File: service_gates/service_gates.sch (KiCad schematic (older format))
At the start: 1 part, among them P1 DIN_41612_128P

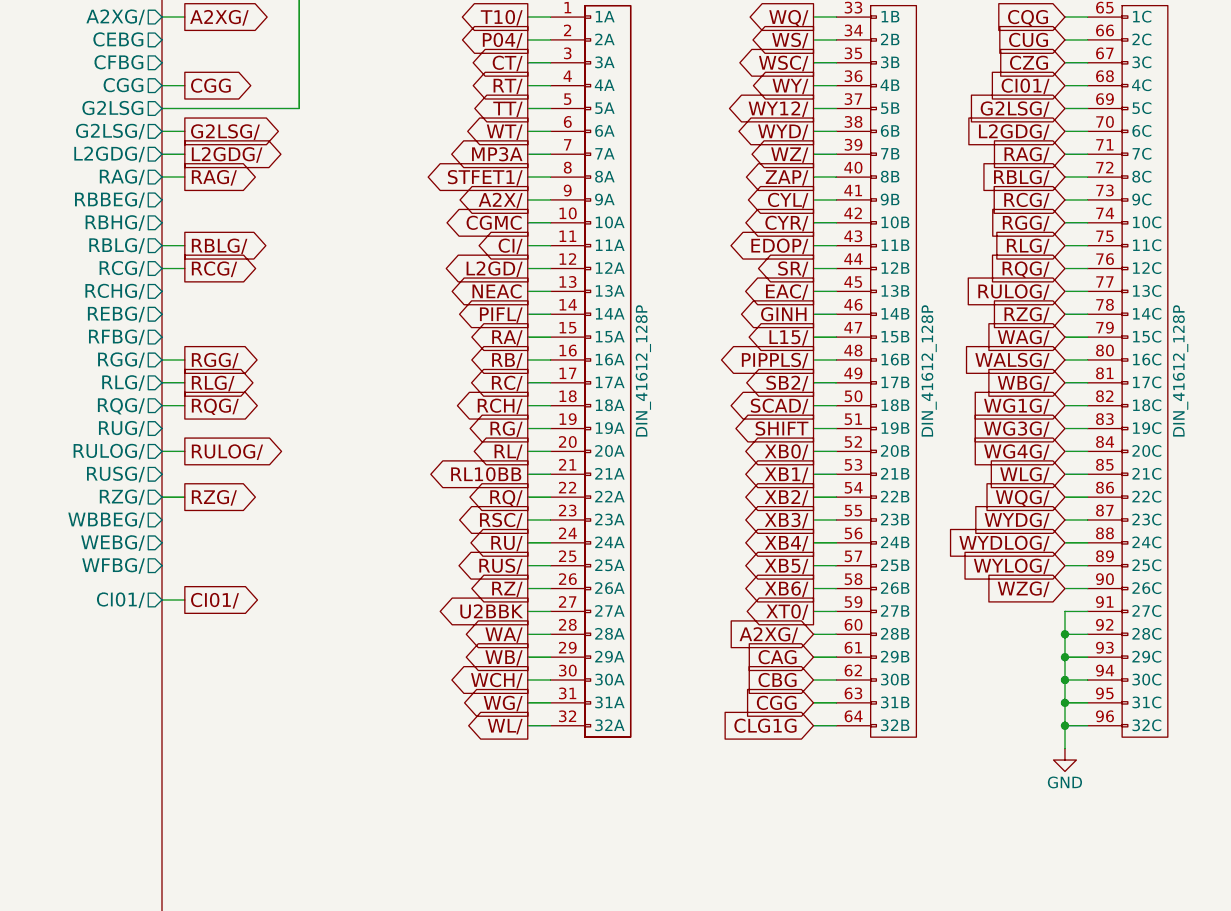
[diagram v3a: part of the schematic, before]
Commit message: Added a fully tied in module 10.
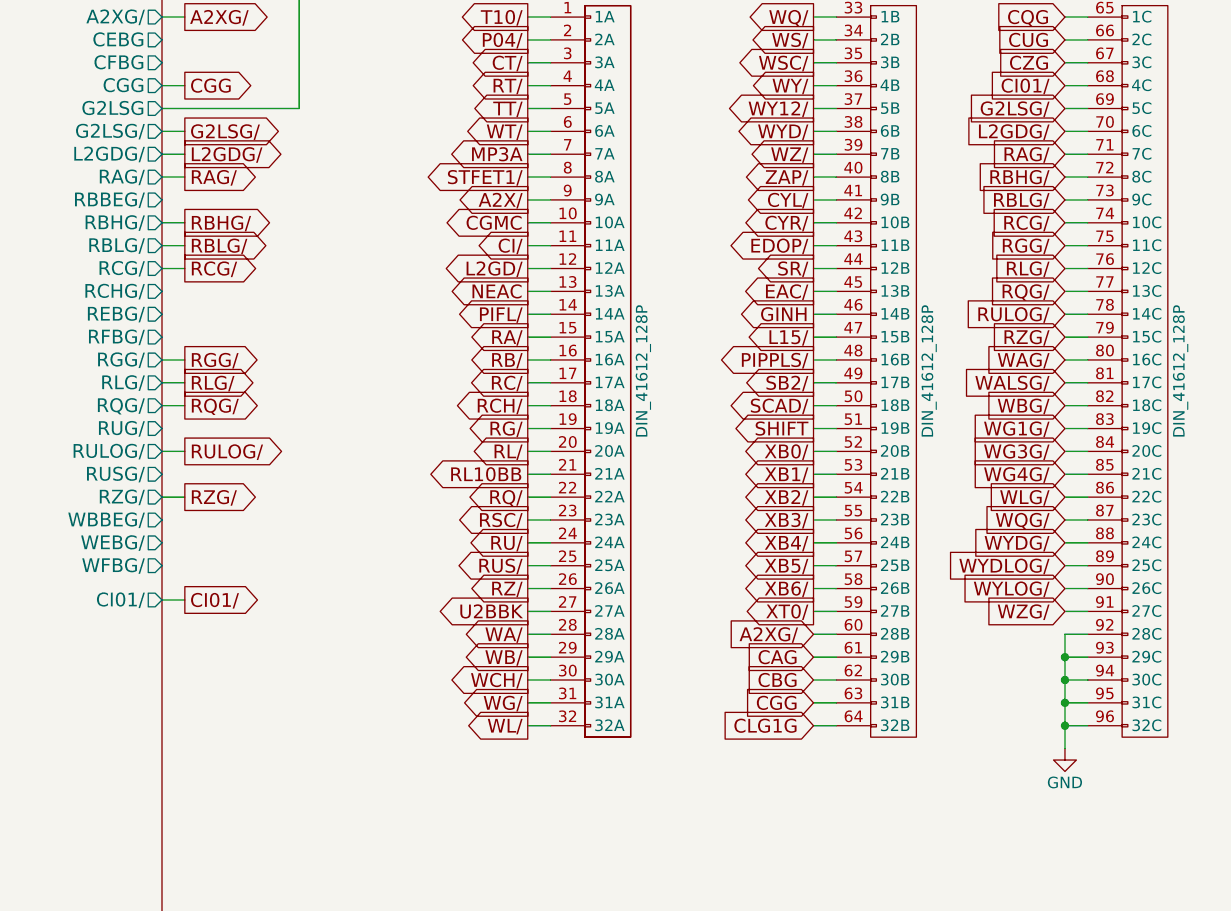
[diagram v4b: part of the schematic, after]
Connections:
- net GND: no longer P1.91 (27C)
- net RBLG/: now also P1.73 (9C); no longer P1.72 (8C)
- net RCG/: now also P1.74 (10C); no longer P1.73 (9C)
- net RGG/: now also P1.75 (11C); no longer P1.74 (10C)
- net RLG/: now also P1.76 (12C); no longer P1.75 (11C)
- net RQG/: now also P1.77 (13C); no longer P1.76 (12C)
- net RULOG/: now also P1.78 (14C); no longer P1.77 (13C)
- net RZG/: now also P1.79 (15C); no longer P1.78 (14C)
- net WAG/: now also P1.80 (16C); no longer P1.79 (15C)
- net WALSG/: now also P1.81 (17C); no longer P1.80 (16C)
- net WBG/: now also P1.82 (18C); no longer P1.81 (17C)
- net WG1G/: now also P1.83 (19C); no longer P1.82 (18C)
- net WG3G/: now also P1.84 (20C); no longer P1.83 (19C)
- net WG4G/: now also P1.85 (21C); no longer P1.84 (20C)
- net WLG/: now also P1.86 (22C); no longer P1.85 (21C)
- net WQG/: now also P1.87 (23C); no longer P1.86 (22C)
- net WYDG/: now also P1.88 (24C); no longer P1.87 (23C)
- net WYDLOG/: now also P1.89 (25C); no longer P1.88 (24C)
- net WYLOG/: now also P1.90 (26C); no longer P1.89 (25C)
- net WZG/: now also P1.91 (27C); no longer P1.90 (26C)
- new net RBHG/: P1.72 (8C)
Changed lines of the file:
@@
 	10600 4150 10700 4150
 Connection ~ 10600 4250
-Wire Wire Line
-	10600 4050 10700 4050
 Connection ~ 10600 4150
 Wire Wire Line
 	10600 3950 10700 3950
-Connection ~ 10600 4050
-Wire Wire Line
-	10600 3850 10700 3850
-Wire Wire Line
-	10600 2650 10700 2650
+Wire Wire Line
+	10600 2750 10700 2750
+Wire Wire Line
+	10600 2550 10700 2550
 Wire Wire Line
 	10600 2450 10700 2450
@@
 Wire Wire Line
 	10600 2250 10700 2250
-Wire Wire Line
-	10600 2150 10700 2150
 $Comp
 L DIN_41612_128P P1
@@
 RBLG/
 Wire Wire Line
-	10600 2050 10700 2050
-Text GLabel 10600 2050 0    60   Input ~ 0
+	10600 2150 10700 2150
+Text GLabel 10600 2150 0    60   Input ~ 0
 RBLG/
 Wire Wire Line
@@
 Text GLabel 6750 2450 2    60   Output ~ 0
 RCG/
-Text GLabel 10600 2150 0    60   Input ~ 0
+Text GLabel 10600 2250 0    60   Input ~ 0
 RCG/
 Wire Wire Line
@@
 Text GLabel 6750 2850 2    60   Output ~ 0
 RGG/
-Text GLabel 10600 2250 0    60   Input ~ 0
+Text GLabel 10600 2350 0    60   Input ~ 0
 RGG/
 Wire Wire Line
@@
 Text GLabel 6750 2950 2    60   Output ~ 0
 RLG/
-Text GLabel 10600 2350 0    60   Input ~ 0
+Text GLabel 10600 2450 0    60   Input ~ 0
 RLG/
 Wire Wire Line
@@
 Text GLabel 6750 3050 2    60   Output ~ 0
 RQG/
-Text GLabel 10600 2450 0    60   Input ~ 0
+Text GLabel 10600 2550 0    60   Input ~ 0
 RQG/
 Wire Wire Line
@@
 RULOG/
 Wire Wire Line
-	10600 2550 10700 2550
-Text GLabel 10600 2550 0    60   Input ~ 0
+	10600 2650 10700 2650
+Text GLabel 10600 2650 0    60   Input ~ 0
 RULOG/
 Wire Wire Line
@@
 Text GLabel 6750 3450 2    60   Output ~ 0
 RZG/
-Text GLabel 10600 2650 0    60   Input ~ 0
+Text GLabel 10600 2750 0    60   Input ~ 0
 RZG/
 Wire Wire Line
@@
 WALSG/
 Wire Wire Line
-	10600 2750 10700 2750
-Text GLabel 10600 2750 0    60   Input ~ 0
-WAG/
-Wire Wire Line
 	10600 2850 10700 2850
 Text GLabel 10600 2850 0    60   Input ~ 0
+WAG/
+Wire Wire Line
+	10600 2950 10700 2950
+Text GLabel 10600 2950 0    60   Input ~ 0
 WALSG/
 Wire Wire Line
@@
 WBG/
 Wire Wire Line
-	10600 2950 10700 2950
-Text GLabel 10600 2950 0    60   Input ~ 0
+	10600 3050 10700 3050
+Text GLabel 10600 3050 0    60   Input ~ 0
 WBG/
 Wire Wire Line
@@
 WG4G/
 Wire Wire Line
-	10600 3050 10700 3050
-Text GLabel 10600 3050 0    60   Input ~ 0
-WG1G/
-Wire Wire Line
 	10600 3150 10700 3150
 Text GLabel 10600 3150 0    60   Input ~ 0
-WG3G/
+WG1G/
 Wire Wire Line
 	10600 3250 10700 3250
 Text GLabel 10600 3250 0    60   Input ~ 0
+WG3G/
+Wire Wire Line
+	10600 3350 10700 3350
+Text GLabel 10600 3350 0    60   Input ~ 0
 WG4G/
 Wire Wire Line
@@
 WLG/
 Wire Wire Line
-	10600 3350 10700 3350
-Text GLabel 10600 3350 0    60   Input ~ 0
-WLG/
-Wire Wire Line
 	10600 3450 10700 3450
 Text GLabel 10600 3450 0    60   Input ~ 0
+WLG/
+Wire Wire Line
+	10600 3550 10700 3550
+Text GLabel 10600 3550 0    60   Input ~ 0
 WQG/
 Wire Wire Line
@@
 WYLOG/
 Wire Wire Line
-	10600 3550 10700 3550
-Text GLabel 10600 3550 0    60   Input ~ 0
-WYDG/
-Wire Wire Line
 	10600 3650 10700 3650
 Text GLabel 10600 3650 0    60   Input ~ 0
-WYDLOG/
+WYDG/
 Wire Wire Line
 	10600 3750 10700 3750
 Text GLabel 10600 3750 0    60   Input ~ 0
+WYDLOG/
+Wire Wire Line
+	10600 3850 10700 3850
+Text GLabel 10600 3850 0    60   Input ~ 0
 WYLOG/
 Wire Wire Line
@@
 WZG/
 Wire Wire Line
-	10600 3950 10600 4550
-Text GLabel 10600 3850 0    60   Input ~ 0
+	10600 4050 10600 4550
+Text GLabel 10600 3950 0    60   Input ~ 0
 WZG/
+Wire Wire Line
+	6650 2250 6750 2250
+Text GLabel 6750 2250 2    60   Output ~ 0
+RBHG/
+Wire Wire Line
+	10600 4050 10700 4050
+Wire Wire Line
+	10600 2050 10700 2050
+Text GLabel 10600 2050 0    60   Input ~ 0
+RBHG/
 $EndSCHEMATC

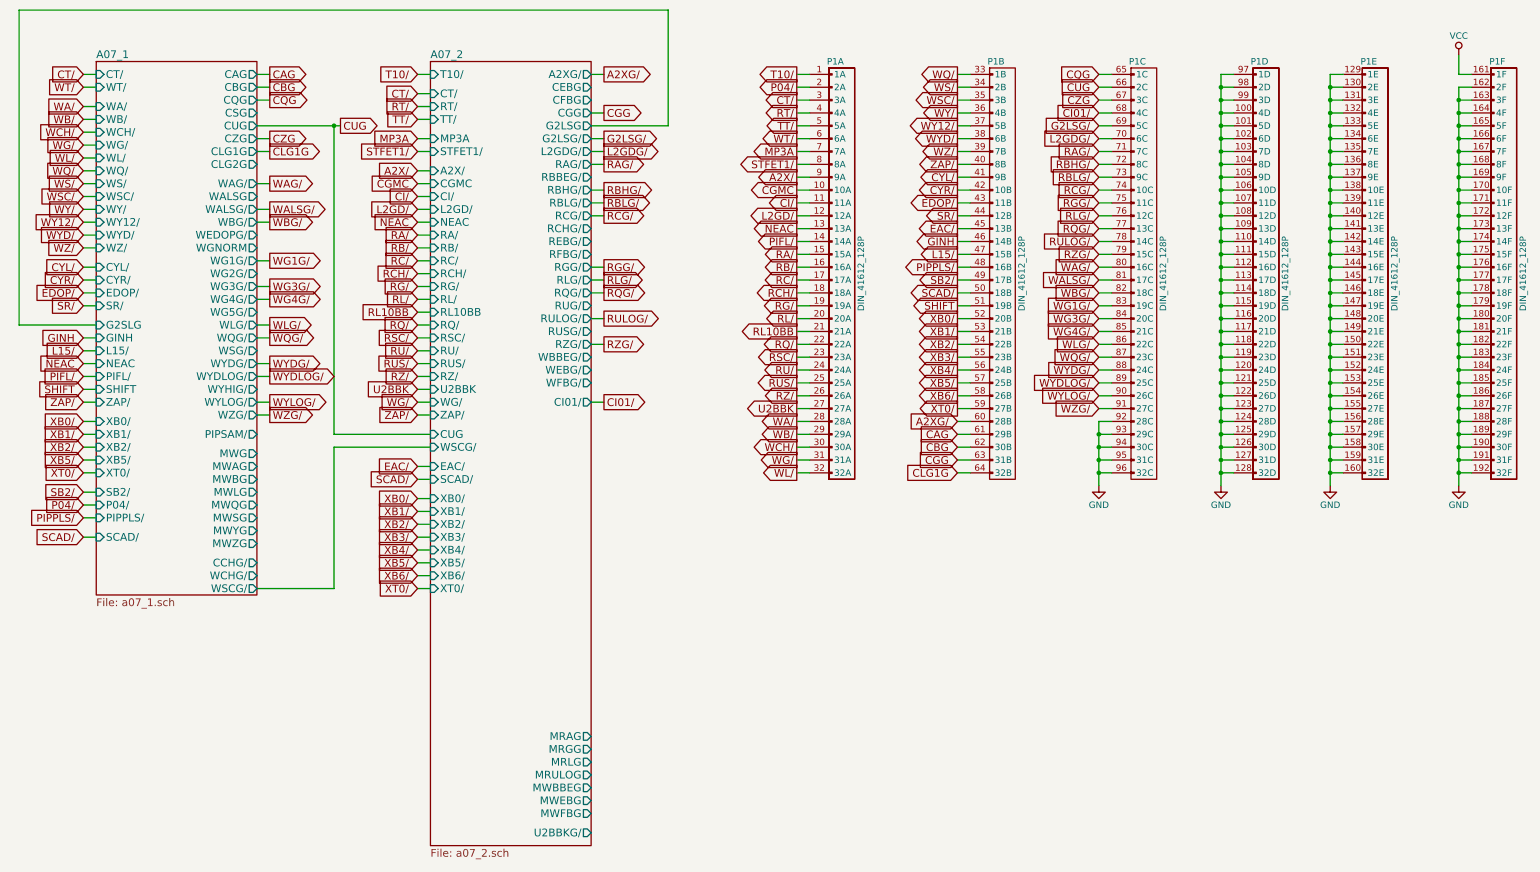
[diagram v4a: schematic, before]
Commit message: Added the final four bit module. All 16 bits of the central/special registers are present. We're stuck at address 0 because TC is using RAD, which needs to be translated into RG or RZ by module 12
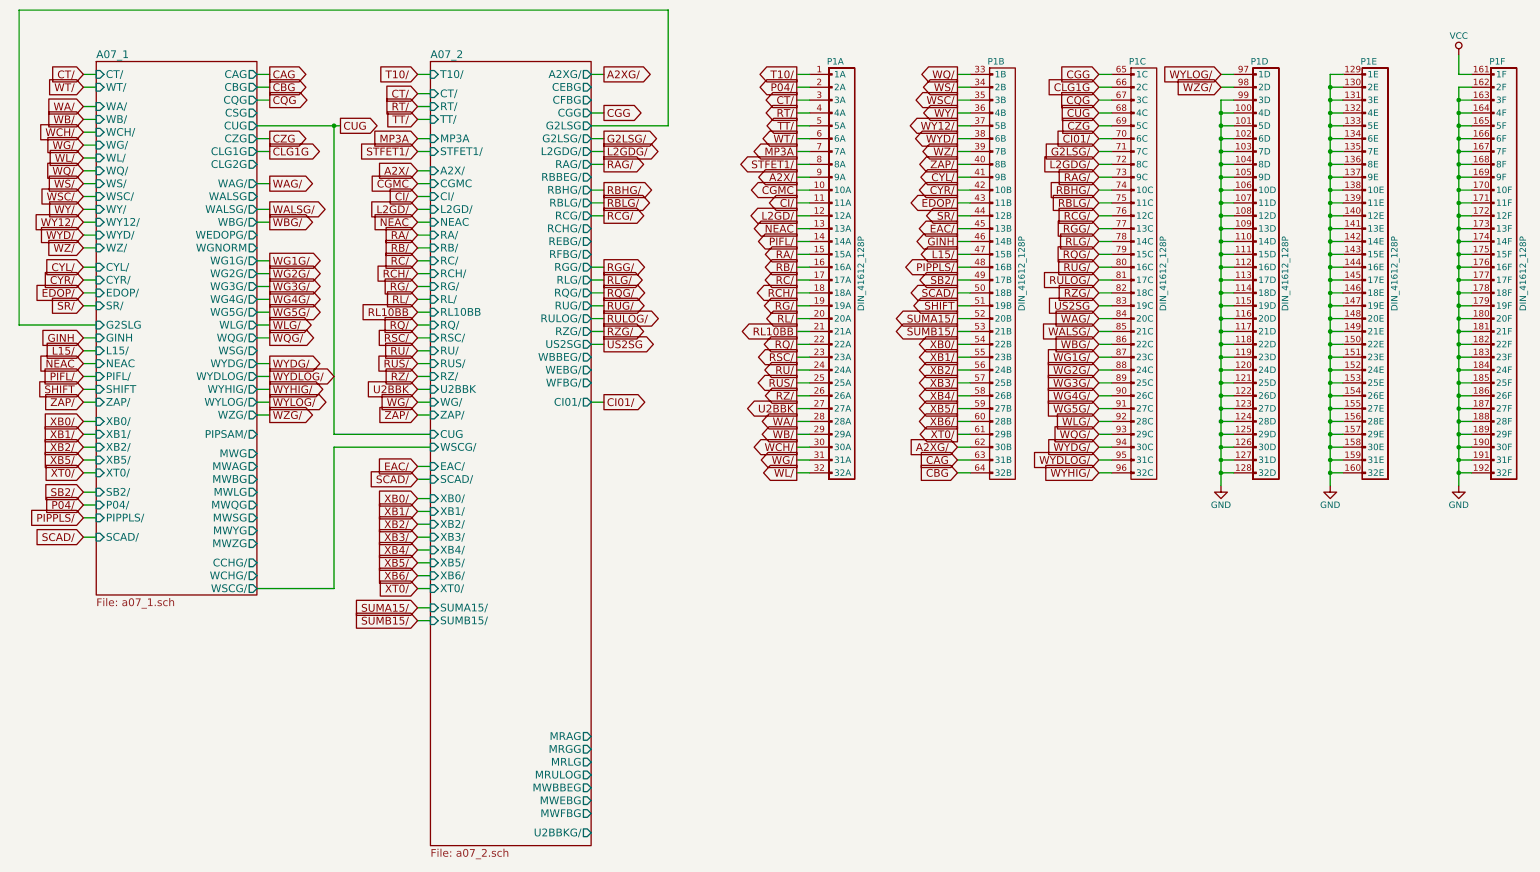
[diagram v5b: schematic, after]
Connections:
- net A2XG/: now also P1.62 (30B); no longer P1.60 (28B)
- net CAG: now also P1.63 (31B); no longer P1.61 (29B)
- net CBG: now also P1.64 (32B); no longer P1.62 (30B)
- net CGG: now also P1.65 (1C); no longer P1.63 (31B)
- net CI01/: now also P1.70 (6C); no longer P1.68 (4C)
- net CLG1G: now also P1.66 (2C); no longer P1.64 (32B)
- net CQG: now also P1.67 (3C); no longer P1.65 (1C)
- net CUG: now also P1.68 (4C); no longer P1.66 (2C)
- net CZG: now also P1.69 (5C); no longer P1.67 (3C)
- net G2LSG/: now also P1.71 (7C); no longer P1.69 (5C)
- net GND: no longer P1.92 (28C), P1.93 (29C), P1.94 (30C), P1.95 (31C), P1.96 (32C), P1.97 (1D), P1.98 (2D)
- net L2GDG/: now also P1.72 (8C); no longer P1.70 (6C)
- net RAG/: now also P1.73 (9C); no longer P1.71 (7C)
- net RBHG/: now also P1.74 (10C); no longer P1.72 (8C)
- net RBLG/: now also P1.75 (11C); no longer P1.73 (9C)
- net RCG/: now also P1.76 (12C); no longer P1.74 (10C)
- net RGG/: now also P1.77 (13C); no longer P1.75 (11C)
- net RLG/: now also P1.78 (14C); no longer P1.76 (12C)
- net RQG/: now also P1.79 (15C); no longer P1.77 (13C)
- net RULOG/: now also P1.81 (17C); no longer P1.78 (14C)
- net RZG/: now also P1.82 (18C); no longer P1.79 (15C)
- net WAG/: now also P1.84 (20C); no longer P1.80 (16C)
- net WALSG/: now also P1.85 (21C); no longer P1.81 (17C)
- net WBG/: now also P1.86 (22C); no longer P1.82 (18C)
- net WG1G/: now also P1.87 (23C); no longer P1.83 (19C)
- net WG3G/: now also P1.89 (25C); no longer P1.84 (20C)
- net WG4G/: now also P1.90 (26C); no longer P1.85 (21C)
- net WLG/: now also P1.92 (28C); no longer P1.86 (22C)
- net WQG/: now also P1.93 (29C); no longer P1.87 (23C)
- net WYDG/: now also P1.94 (30C); no longer P1.88 (24C)
- net WYDLOG/: now also P1.95 (31C); no longer P1.89 (25C)
- net WYLOG/: now also P1.97 (1D); no longer P1.90 (26C)
- net WZG/: now also P1.98 (2D); no longer P1.91 (27C)
- net XB0/: now also P1.54 (22B); no longer P1.52 (20B)
- net XB1/: now also P1.55 (23B); no longer P1.53 (21B)
- net XB2/: now also P1.56 (24B); no longer P1.54 (22B)
- net XB3/: now also P1.57 (25B); no longer P1.55 (23B)
- net XB4/: now also P1.58 (26B); no longer P1.56 (24B)
- net XB5/: now also P1.59 (27B); no longer P1.57 (25B)
- net XB6/: now also P1.60 (28B); no longer P1.58 (26B)
- net XT0/: now also P1.61 (29B); no longer P1.59 (27B)
- new net RUG/: P1.80 (16C)
- new net SUMA15/: P1.52 (20B)
- new net SUMB15/: P1.53 (21B)
- new net US2SG: P1.83 (19C)
- new net WG2G/: P1.88 (24C)
- new net WG5G/: P1.91 (27C)
- new net WYHIG/: P1.96 (32C)
